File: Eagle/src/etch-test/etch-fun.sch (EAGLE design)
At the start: 2 parts

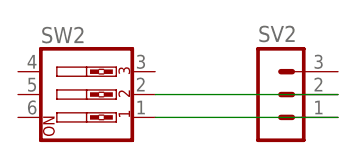
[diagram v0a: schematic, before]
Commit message: Update etch-fun.sch
small test PCB
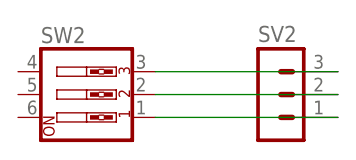
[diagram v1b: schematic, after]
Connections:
- new net N$3: SV2.3, SW2.3
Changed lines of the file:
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@@
 </variantdefs>
 <classes>
-<class number="0" name="default" width="0" drill="0">
+<class number="0" name="default" width="0.254" drill="0">
+</class>
+<class number="1" name="test1" width="0.3048" drill="0">
 </class>
 </classes>
@@
 <pinref part="SV2" gate="G$1" pin="1"/>
 <pinref part="SW2" gate="A" pin="1"/>
-<wire x1="60.96" y1="58.42" x2="40.64" y2="58.42" width="0.1524" layer="91"/>
+<wire x1="60.96" y1="58.42" x2="40.64" y2="58.42" width="0.3048" layer="91"/>
 </segment>
 </net>
@@
 <pinref part="SW2" gate="A" pin="2"/>
 <pinref part="SV2" gate="G$1" pin="2"/>
-<wire x1="40.64" y1="60.96" x2="60.96" y2="60.96" width="0.1524" layer="91"/>
+<wire x1="40.64" y1="60.96" x2="60.96" y2="60.96" width="0.3048" layer="91"/>
 </segment>
 </net>
+<net name="N$3" class="0">
+<segment>
+<pinref part="SV2" gate="G$1" pin="3"/>
+<pinref part="SW2" gate="A" pin="3"/>
+<wire x1="60.96" y1="63.5" x2="40.64" y2="63.5" width="0.3048" layer="91"/>
+</segment>
+</net>
